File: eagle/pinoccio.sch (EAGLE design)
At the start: 60 parts, among them IC1 ATMEGA16U2QFN32, J1 AVR_SPI_PRG_6, Q1 16MHz, Q2 32.768k, Q3 16MHz, U1 MCP73831, U2 TPS78233, U4 ATMEGA128RFA1, X1 USB-MICROB, Y2 ANTENNA2SMD5

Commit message: Moar fixups
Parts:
- C2: value 1.0uF -> 2.2uF
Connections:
- net VCC: now also U$3.VIN1; no longer U$3.P1-VIN1
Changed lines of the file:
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@@
 <parts>
 <part name="FRAME1" library="Pinoccio" deviceset="FRAME-LETTER" device=""/>
-<part name="C2" library="Pinoccio" deviceset="CAP" device="0402-CAP" value="1.0uF"/>
+<part name="C2" library="Pinoccio" deviceset="CAP" device="0402-CAP" value="2.2uF"/>
 <part name="JP4" library="Pinoccio" deviceset="AVR_SPI_PRG_6" device="" value="AVR_SPI"/>
 <part name="P+1" library="SparkFun" deviceset="VCC" device=""/>
@@
 </segment>
 <segment>
-<pinref part="U$3" gate="G$1" pin="P1-VIN1"/>
+<pinref part="U$3" gate="G$1" pin="VIN1"/>
 <wire x1="210.82" y1="55.88" x2="208.28" y2="55.88" width="0.1524" layer="91"/>
 <label x="195.58" y="55.88" size="1.778" layer="95"/>

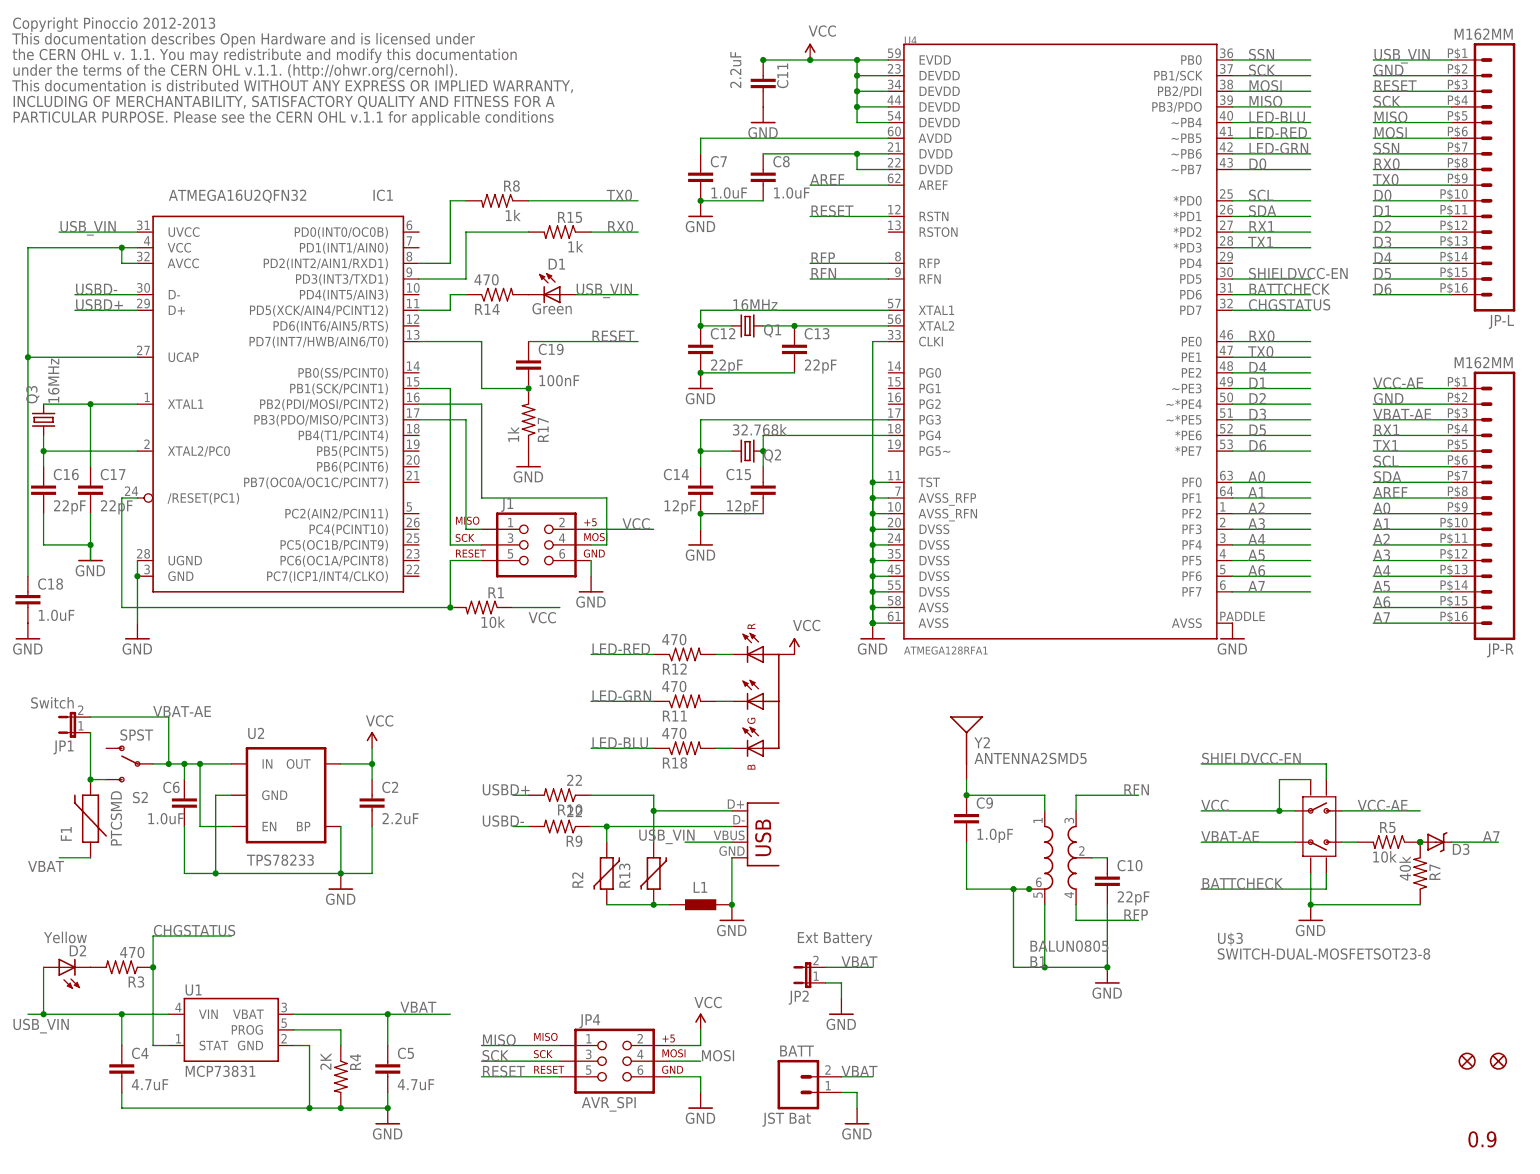
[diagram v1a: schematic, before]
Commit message: Fix up library naming
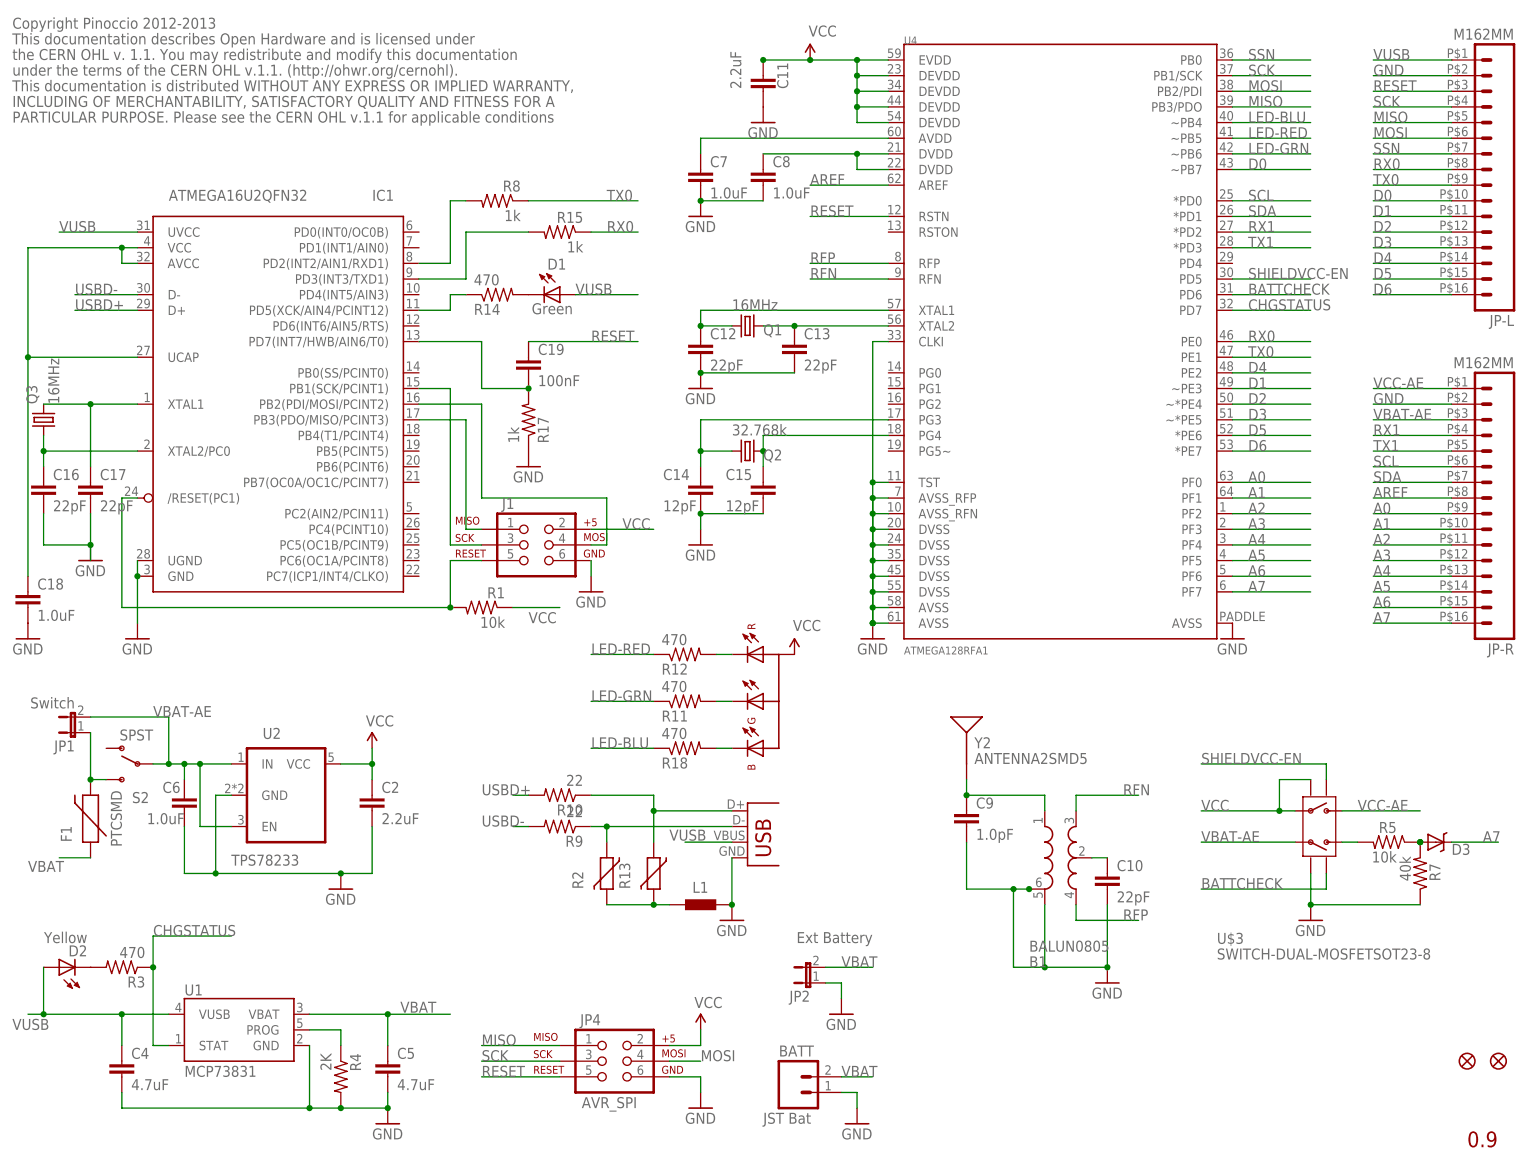
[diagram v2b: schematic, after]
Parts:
- D3: value DIODE-SCHOTTKY -> DIODE-SCHOTTKY0402; device Pinoccio:DIODE-SCHOTTKY -> Pinoccio:DIODE-SCHOTTKY0402
- U2: device SparkFun:V_REG_LDOSMD -> Pinoccio:LDO-TPS78233
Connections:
- removed net USB_VIN: C4.1, D1.A, D2.A, IC1.UVCC, JP-L.1, U1.VIN, X1.VBUS
- new net VUSB: C4.1, D1.A, D2.A, IC1.UVCC, JP-L.1, U1.VUSB, X1.VBUS
- net GND: no longer U2.BP
- net VCC: now also U2.VCC; no longer U2.OUT
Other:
- moved on the sheet: U1
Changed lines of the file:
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@@
 <part name="GND1" library="SparkFun" deviceset="GND" device=""/>
 <part name="P+4" library="SparkFun" deviceset="VCC" device=""/>
-<part name="U2" library="SparkFun" deviceset="V_REG_LDO" device="SMD" value="TPS78233"/>
+<part name="U2" library="Pinoccio" deviceset="LDO-TPS78233" device="" value="TPS78233"/>
 <part name="C4" library="Pinoccio" deviceset="CAP" device="0402-CAP" value="4.7uF"/>
 <part name="C5" library="Pinoccio" deviceset="CAP" device="0402-CAP" value="4.7uF"/>
@@
 <part name="R8" library="Pinoccio" deviceset="RESISTOR" device="0402-RES" value="1k"/>
 <part name="R15" library="Pinoccio" deviceset="RESISTOR" device="0402-RES" value="1k"/>
-<part name="D3" library="Pinoccio" deviceset="DIODE-SCHOTTKY" device=""/>
+<part name="D3" library="Pinoccio" deviceset="DIODE-SCHOTTKY" device="0402"/>
 <part name="U$3" library="Pinoccio" deviceset="SWITCH-DUAL-MOSFET" device="SOT23-8"/>
 <part name="GND7" library="SparkFun" deviceset="GND" device=""/>
@@
 <wire x1="50.8" y1="7.62" x2="55.88" y2="7.62" width="0.1524" layer="91"/>
 <wire x1="55.88" y1="7.62" x2="63.5" y2="7.62" width="0.1524" layer="91"/>
-<wire x1="48.26" y1="17.78" x2="50.8" y2="17.78" width="0.1524" layer="91"/>
 <wire x1="50.8" y1="17.78" x2="50.8" y2="7.62" width="0.1524" layer="91"/>
 <pinref part="U1" gate="G$1" pin="GND"/>
@@
 <wire x1="35.56" y1="58.42" x2="35.56" y2="45.72" width="0.1524" layer="91"/>
 <junction x="35.56" y="45.72"/>
-<pinref part="U2" gate="G$1" pin="BP"/>
-<wire x1="55.88" y1="53.34" x2="55.88" y2="45.72" width="0.1524" layer="91"/>
 </segment>
 <segment>
@@
 </segment>
 <segment>
-<wire x1="55.88" y1="63.5" x2="60.96" y2="63.5" width="0.1524" layer="91"/>
-<wire x1="60.96" y1="66.04" x2="60.96" y2="63.5" width="0.1524" layer="91"/>
-<wire x1="60.96" y1="63.5" x2="60.96" y2="60.96" width="0.1524" layer="91"/>
-<junction x="60.96" y="63.5"/>
-<pinref part="U2" gate="G$1" pin="OUT"/>
-<pinref part="C2" gate="G$1" pin="1"/>
-<pinref part="P+4" gate="1" pin="VCC"/>
-</segment>
-<segment>
 <pinref part="P+3" gate="1" pin="VCC"/>
 <wire x1="139.7" y1="177.8" x2="132.08" y2="177.8" width="0.1524" layer="91"/>
@@
 <label x="101.6" y="101.6" size="1.778" layer="95"/>
 </segment>
+<segment>
+<pinref part="U2" gate="G$1" pin="VCC"/>
+<wire x1="55.88" y1="63.5" x2="60.96" y2="63.5" width="0.1524" layer="91"/>
+<pinref part="P+4" gate="1" pin="VCC"/>
+<wire x1="60.96" y1="63.5" x2="60.96" y2="66.04" width="0.1524" layer="91"/>
+<pinref part="C2" gate="G$1" pin="1"/>
+<wire x1="60.96" y1="60.96" x2="60.96" y2="63.5" width="0.1524" layer="91"/>
+<junction x="60.96" y="63.5"/>
+</segment>
 </net>
 <net name="MOSI" class="0">
@@
 </segment>
 </net>
-<net name="USB_VIN" class="0">
+<net name="VUSB" class="0">
 <segment>
 <wire x1="119.38" y1="50.8" x2="111.76" y2="50.8" width="0.1524" layer="91"/>
-<label x="104.14" y="51.054" size="1.778" layer="95"/>
+<label x="109.22" y="51.054" size="1.778" layer="95"/>
 <pinref part="X1" gate="G$1" pin="VBUS"/>
 </segment>
 <segment>
 <wire x1="7.62" y1="22.86" x2="20.32" y2="22.86" width="0.1524" layer="91"/>
-<wire x1="20.32" y1="22.86" x2="27.94" y2="22.86" width="0.1524" layer="91"/>
 <wire x1="20.32" y1="17.78" x2="20.32" y2="22.86" width="0.1524" layer="91"/>
 <wire x1="7.62" y1="30.48" x2="7.62" y2="22.86" width="0.1524" layer="91"/>
-<junction x="20.32" y="22.86"/>
 <label x="2.54" y="20.32" size="1.778" layer="95"/>
-<pinref part="U1" gate="G$1" pin="VIN"/>
 <pinref part="C4" gate="G$1" pin="1"/>
 <pinref part="D2" gate="G$1" pin="A"/>
 <wire x1="7.62" y1="22.86" x2="5.08" y2="22.86" width="0.1524" layer="91"/>
 <junction x="7.62" y="22.86"/>
+<pinref part="U1" gate="G$1" pin="VUSB"/>
+<wire x1="20.32" y1="22.86" x2="27.94" y2="22.86" width="0.1524" layer="91"/>
+<junction x="20.32" y="22.86"/>
 </segment>
 <segment>
@@
 <wire x1="63.5" y1="22.86" x2="73.66" y2="22.86" width="0.1524" layer="91"/>
 <wire x1="63.5" y1="17.78" x2="63.5" y2="22.86" width="0.1524" layer="91"/>
-<wire x1="48.26" y1="22.86" x2="63.5" y2="22.86" width="0.1524" layer="91"/>
+<wire x1="50.8" y1="22.86" x2="63.5" y2="22.86" width="0.1524" layer="91"/>
 <junction x="63.5" y="22.86"/>
 <label x="65.532" y="23.114" size="1.778" layer="95"/>
@@
 <net name="N$11" class="0">
 <segment>
-<wire x1="48.26" y1="20.32" x2="55.88" y2="20.32" width="0.1524" layer="91"/>
+<wire x1="50.8" y1="20.32" x2="55.88" y2="20.32" width="0.1524" layer="91"/>
 <wire x1="55.88" y1="20.32" x2="55.88" y2="17.78" width="0.1524" layer="91"/>
 <pinref part="U1" gate="G$1" pin="PROG"/>
@@
 </sheet>
 </sheets>
-<errors>
-</errors>
 </schematic>
 </drawing>

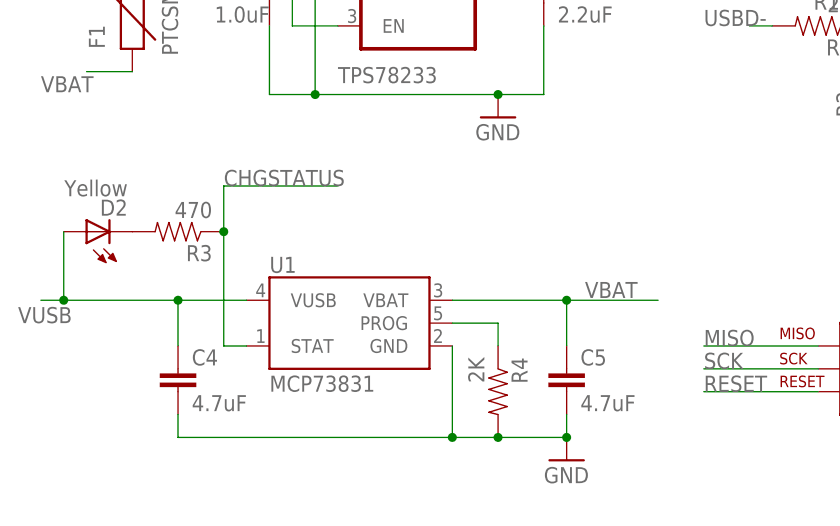
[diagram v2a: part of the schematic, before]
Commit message: move charge LED anode side to vbat instead of vusb
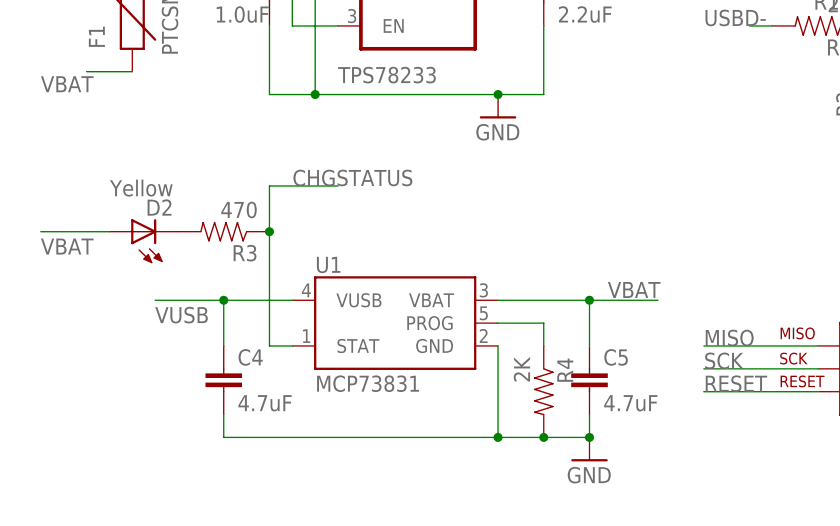
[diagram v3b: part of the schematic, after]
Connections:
- net VBAT: now also D2.A
- net VUSB: no longer D2.A
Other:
- moved on the sheet: C4, C5, D2, R3, R4, U1
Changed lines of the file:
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@@
 </instance>
 <instance part="U2" gate="G$1" x="48.26" y="58.42"/>
-<instance part="C4" gate="G$1" x="20.32" y="12.7"/>
-<instance part="C5" gate="G$1" x="63.5" y="12.7"/>
-<instance part="GND20" gate="1" x="63.5" y="5.08"/>
-<instance part="D2" gate="G$1" x="10.16" y="30.48" rot="R90"/>
-<instance part="R3" gate="G$1" x="20.32" y="30.48" rot="R180"/>
+<instance part="C4" gate="G$1" x="25.4" y="12.7"/>
+<instance part="C5" gate="G$1" x="66.04" y="12.7"/>
+<instance part="GND20" gate="1" x="66.04" y="5.08"/>
+<instance part="D2" gate="G$1" x="15.24" y="30.48" rot="R90"/>
+<instance part="R3" gate="G$1" x="25.4" y="30.48" rot="R180"/>
 <instance part="X1" gate="G$1" x="121.92" y="48.26"/>
 <instance part="GND21" gate="1" x="119.38" y="38.1"/>
 <instance part="F1" gate="G$1" x="15.24" y="53.34" rot="R90"/>
 <instance part="S2" gate="1" x="22.86" y="63.5" rot="MR0"/>
-<instance part="U1" gate="G$1" x="38.1" y="20.32"/>
-<instance part="R4" gate="G$1" x="55.88" y="12.7" rot="R270"/>
+<instance part="U1" gate="G$1" x="43.18" y="20.32"/>
+<instance part="R4" gate="G$1" x="60.96" y="12.7" rot="R270"/>
 <instance part="U4" gate="G$1" x="172.72" y="137.16"/>
 <instance part="C7" gate="G$1" x="114.3" y="157.48"/>
@@
 </segment>
 <segment>
-<wire x1="63.5" y1="7.62" x2="63.5" y2="10.16" width="0.1524" layer="91"/>
+<wire x1="66.04" y1="7.62" x2="66.04" y2="10.16" width="0.1524" layer="91"/>
 <pinref part="GND20" gate="1" pin="GND"/>
 <pinref part="C5" gate="G$1" pin="2"/>
 <pinref part="C4" gate="G$1" pin="2"/>
-<wire x1="20.32" y1="7.62" x2="20.32" y2="10.16" width="0.1524" layer="91"/>
-<wire x1="20.32" y1="7.62" x2="50.8" y2="7.62" width="0.1524" layer="91"/>
-<wire x1="50.8" y1="7.62" x2="55.88" y2="7.62" width="0.1524" layer="91"/>
-<wire x1="55.88" y1="7.62" x2="63.5" y2="7.62" width="0.1524" layer="91"/>
-<wire x1="50.8" y1="17.78" x2="50.8" y2="7.62" width="0.1524" layer="91"/>
+<wire x1="25.4" y1="7.62" x2="25.4" y2="10.16" width="0.1524" layer="91"/>
+<wire x1="25.4" y1="7.62" x2="55.88" y2="7.62" width="0.1524" layer="91"/>
+<wire x1="55.88" y1="7.62" x2="60.96" y2="7.62" width="0.1524" layer="91"/>
+<wire x1="60.96" y1="7.62" x2="66.04" y2="7.62" width="0.1524" layer="91"/>
+<wire x1="55.88" y1="17.78" x2="55.88" y2="7.62" width="0.1524" layer="91"/>
 <pinref part="U1" gate="G$1" pin="GND"/>
-<junction x="50.8" y="7.62"/>
+<junction x="55.88" y="7.62"/>
 <pinref part="R4" gate="G$1" pin="2"/>
-<junction x="55.88" y="7.62"/>
-<junction x="63.5" y="7.62"/>
+<junction x="60.96" y="7.62"/>
+<junction x="66.04" y="7.62"/>
 </segment>
 <segment>
@@
 </segment>
 <segment>
-<wire x1="7.62" y1="22.86" x2="20.32" y2="22.86" width="0.1524" layer="91"/>
-<wire x1="20.32" y1="17.78" x2="20.32" y2="22.86" width="0.1524" layer="91"/>
-<wire x1="7.62" y1="30.48" x2="7.62" y2="22.86" width="0.1524" layer="91"/>
-<label x="2.54" y="20.32" size="1.778" layer="95"/>
+<wire x1="25.4" y1="17.78" x2="25.4" y2="22.86" width="0.1524" layer="91"/>
+<label x="17.78" y="20.32" size="1.778" layer="95"/>
 <pinref part="C4" gate="G$1" pin="1"/>
-<pinref part="D2" gate="G$1" pin="A"/>
-<wire x1="7.62" y1="22.86" x2="5.08" y2="22.86" width="0.1524" layer="91"/>
-<junction x="7.62" y="22.86"/>
+<wire x1="25.4" y1="22.86" x2="17.78" y2="22.86" width="0.1524" layer="91"/>
 <pinref part="U1" gate="G$1" pin="VUSB"/>
-<wire x1="20.32" y1="22.86" x2="27.94" y2="22.86" width="0.1524" layer="91"/>
-<junction x="20.32" y="22.86"/>
+<wire x1="25.4" y1="22.86" x2="33.02" y2="22.86" width="0.1524" layer="91"/>
+<junction x="25.4" y="22.86"/>
 </segment>
 <segment>
@@
 <net name="VBAT" class="0">
 <segment>
-<wire x1="63.5" y1="22.86" x2="73.66" y2="22.86" width="0.1524" layer="91"/>
-<wire x1="63.5" y1="17.78" x2="63.5" y2="22.86" width="0.1524" layer="91"/>
-<wire x1="50.8" y1="22.86" x2="63.5" y2="22.86" width="0.1524" layer="91"/>
-<junction x="63.5" y="22.86"/>
-<label x="65.532" y="23.114" size="1.778" layer="95"/>
+<wire x1="66.04" y1="22.86" x2="73.66" y2="22.86" width="0.1524" layer="91"/>
+<wire x1="66.04" y1="17.78" x2="66.04" y2="22.86" width="0.1524" layer="91"/>
+<wire x1="55.88" y1="22.86" x2="66.04" y2="22.86" width="0.1524" layer="91"/>
+<junction x="66.04" y="22.86"/>
+<label x="68.072" y="23.114" size="1.778" layer="95"/>
 <pinref part="C5" gate="G$1" pin="1"/>
 <pinref part="U1" gate="G$1" pin="VBAT"/>
@@
 <wire x1="137.16" y1="12.7" x2="142.24" y2="12.7" width="0.1524" layer="91"/>
 <label x="137.16" y="12.7" size="1.778" layer="95"/>
+</segment>
+<segment>
+<pinref part="D2" gate="G$1" pin="A"/>
+<wire x1="12.7" y1="30.48" x2="5.08" y2="30.48" width="0.1524" layer="91"/>
+<label x="5.08" y="27.94" size="1.778" layer="95"/>
 </segment>
 </net>
@@
 <net name="N$11" class="0">
 <segment>
-<wire x1="50.8" y1="20.32" x2="55.88" y2="20.32" width="0.1524" layer="91"/>
-<wire x1="55.88" y1="20.32" x2="55.88" y2="17.78" width="0.1524" layer="91"/>
+<wire x1="55.88" y1="20.32" x2="60.96" y2="20.32" width="0.1524" layer="91"/>
+<wire x1="60.96" y1="20.32" x2="60.96" y2="17.78" width="0.1524" layer="91"/>
 <pinref part="U1" gate="G$1" pin="PROG"/>
 <pinref part="R4" gate="G$1" pin="1"/>
@@
 <net name="CHGSTATUS" class="0">
 <segment>
-<wire x1="25.4" y1="35.56" x2="38.1" y2="35.56" width="0.1524" layer="91"/>
-<label x="25.4" y="35.56" size="1.778" layer="95"/>
-<wire x1="27.94" y1="17.78" x2="25.4" y2="17.78" width="0.1524" layer="91"/>
-<wire x1="25.4" y1="17.78" x2="25.4" y2="30.48" width="0.1524" layer="91"/>
+<wire x1="30.48" y1="35.56" x2="38.1" y2="35.56" width="0.1524" layer="91"/>
+<label x="33.02" y="35.56" size="1.778" layer="95"/>
+<wire x1="33.02" y1="17.78" x2="30.48" y2="17.78" width="0.1524" layer="91"/>
+<wire x1="30.48" y1="17.78" x2="30.48" y2="30.48" width="0.1524" layer="91"/>
 <pinref part="U1" gate="G$1" pin="STAT"/>
 <pinref part="R3" gate="G$1" pin="1"/>
-<wire x1="25.4" y1="35.56" x2="25.4" y2="30.48" width="0.1524" layer="91"/>
-<junction x="25.4" y="30.48"/>
-</segment>
-<segment>
+<wire x1="30.48" y1="35.56" x2="30.48" y2="30.48" width="0.1524" layer="91"/>
+<junction x="30.48" y="30.48"/>
+</segment>
+<segment>
